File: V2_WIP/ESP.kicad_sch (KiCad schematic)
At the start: 36 parts, among them J202 USB4145-03-0230-C, Q1 IRLML5203, Q2 S8050, Q3 S8050, SW2 PTS647SN70SMTR2N LFS, U1 ESP32-WROOM-32UE, U14 *CH340K, U201 RT9080-33GJ5

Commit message: updated list of changes in README.md
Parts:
- added R108: 1k, Resistor_SMD:R_0603_1608Metric_Pad0.98x0.95mm_HandSolder, symbol Device:R
- TP201: footprint TestPoint:TestPoint_Pad_D1.5mm -> TestPoint:TestPoint_Pad_D1.0mm
- TP202: value VCC -> LDO_VCC; footprint TestPoint:TestPoint_Pad_D1.5mm -> TestPoint:TestPoint_Pad_D1.0mm
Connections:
- net +3V3: now also R108.2
- net GND: now also J202.B8 (SBU2); no longer J202.B5 (CC2)
- net at R205.2: now also J202.B5 (CC2); no longer J202.B8 (SBU2)
- net at U1.29 (IO5): now also R108.1
- no-connect marks 6 -> 5
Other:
- note added: "ENC CLK"
- note added: "ENC DT"
- note added: "ENC SW"
- note added: "GNSS TX"
- note added: "GNSSRX"
- note added: "LED"
- note added: "LIGHT_SENS"
- note added: "PULSE"
- note added: "RGB_DATA"
- note added: "RTS"
- note added: "SEL_FL"
- note added: "SEL_IMU"
- note added: "SW2"
- note added: "TP12"
- moved on the sheet: D7, Q3

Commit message: reworked the schematic, changed differential pairs and RF traces, small PCB adjustments
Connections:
- net D+ renamed D_P
- net D- renamed D_N
- net RXD0 renamed RxD0
- net TXD0 renamed TxD0
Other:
- moved on the sheet: C2, C203, C204

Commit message: added second LDO
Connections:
- net IO34: now reaches U1.6 (IO34)
- net IO33: now reaches U1.9 (IO33)
- net +3V3 renamed +3V3_ESP
- no-connect marks 5 -> 3
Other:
- note added: "IMU_INT"
- note added: "LDO_EN"
- moved on the sheet: C11, C201, C202, C3, D3, D4, Q1, R11, R12, TP202, U201

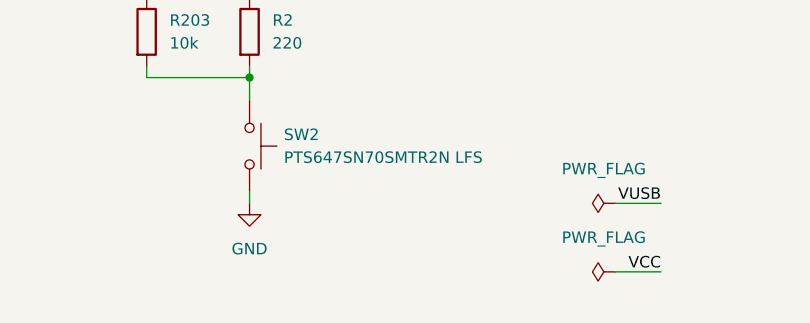
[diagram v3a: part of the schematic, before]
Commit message: switched Tx and Rx on GNSS module, added option to switch them, minor pcb changes
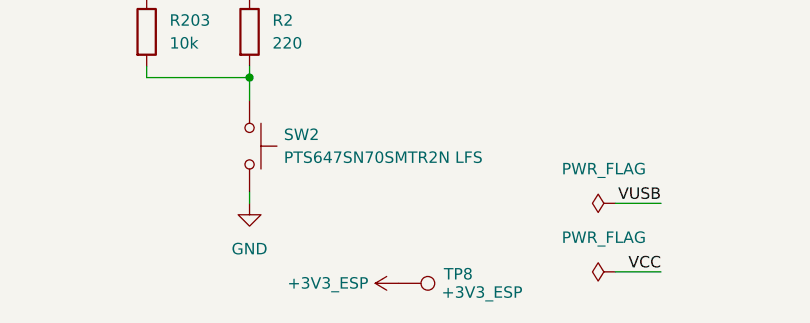
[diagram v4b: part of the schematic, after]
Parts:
- added TP8: +3V3_ESP, TestPoint:TestPoint_Pad_D1.0mm, symbol Connector:TestPoint
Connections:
- net +3V3_ESP: now also TP8.1
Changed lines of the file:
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@@
 	)
 	(symbol
+		(lib_id "Connector:TestPoint")
+		(at 144.78 191.77 270)
+		(unit 1)
+		(body_style 1)
+		(exclude_from_sim no)
+		(in_bom yes)
+		(on_board yes)
+		(in_pos_files yes)
+		(dnp no)
+		(property "Reference" "TP8"
+			(at 149.86 190.754 90)
+			(show_name no)
+			(do_not_autoplace no)
+			(effects
+				(font
+					(size 1.27 1.27)
+				)
+				(justify left)
+			)
+		)
+		(property "Value" "+3V3_ESP"
+			(at 149.606 192.786 90)
+			(show_name no)
+			(do_not_autoplace no)
+			(effects
+				(font
+					(size 1.27 1.27)
+				)
+				(justify left)
+			)
+		)
+		(property "Footprint" "TestPoint:TestPoint_Pad_D1.0mm"
+			(at 144.78 196.85 0)
+			(hide yes)
+			(show_name no)
+			(do_not_autoplace no)
+			(effects
+				(font
+					(size 1.27 1.27)
+				)
+			)
+		)
+		(property "Datasheet" ""
+			(at 144.78 196.85 0)
+			(hide yes)
+			(show_name no)
+			(do_not_autoplace no)
+			(effects
+				(font
+					(size 1.27 1.27)
+				)
+			)
+		)
+		(property "Description" "test point"
+			(at 144.78 191.77 0)
+			(hide yes)
+			(show_name no)
+			(do_not_autoplace no)
+			(effects
+				(font
+					(size 1.27 1.27)
+				)
+			)
+		)
+		(property "Purchase-URL" ""
+			(at 144.78 191.77 0)
+			(hide yes)
+			(show_name no)
+			(do_not_autoplace no)
+			(effects
+				(font
+					(size 1.27 1.27)
+				)
+			)
+		)
+		(pin "1"
+		)
+		(instances
+			(project "gps"
+				(path "/00526ddc-5304-4072-af1e-192a9e7e83da/9ca8f2f0-17b3-4db3-a6cc-93c49e56ea8b"
+					(reference "TP8")
+					(unit 1)
+				)
+			)
+		)
+	)
+	(symbol
 		(lib_id "power:GND")
 		(at 57.15 184.15 0)
@@
 					(unit 1)
 				)
+			)
+		)
+	)
+	(symbol
+		(lib_id "power:+3V3")
+		(at 144.78 191.77 90)
+		(unit 1)
+		(body_style 1)
+		(exclude_from_sim no)
+		(in_bom yes)
+		(on_board yes)
+		(in_pos_files yes)
+		(dnp no)
+		(property "Reference" "#PWR0167"
+			(at 148.59 191.77 0)
+			(hide yes)
+			(show_name no)
+			(do_not_autoplace no)
+			(effects
+				(font
+					(size 1.27 1.27)
+				)
+			)
+		)
+		(property "Value" "+3V3_ESP"
+			(at 141.478 191.77 90)
+			(show_name no)
+			(do_not_autoplace no)
+			(effects
+				(font
+					(size 1.27 1.27)
+				)
+				(justify left)
+			)
+		)
+		(property "Footprint" ""
+			(at 144.78 191.77 0)
+			(hide yes)
+			(show_name no)
+			(do_not_autoplace no)
+			(effects
+				(font
+					(size 1.27 1.27)
+				)
+			)
+		)
+		(property "Datasheet" ""
+			(at 144.78 191.77 0)
+			(hide yes)
+			(show_name no)
+			(do_not_autoplace no)
+			(effects
+				(font
+					(size 1.27 1.27)
+				)
+			)
+		)
+		(property "Description" "Power symbol creates a global label with name \"+3V3\""
+			(at 144.78 191.77 0)
+			(hide yes)
+			(show_name no)
+			(do_not_autoplace no)
+			(effects
+				(font
+					(size 1.27 1.27)
+				)
+			)
+		)
+		(pin "1"
+		)
+		(instances
+			(project "gps"
+				(path "/00526ddc-5304-4072-af1e-192a9e7e83da/9ca8f2f0-17b3-4db3-a6cc-93c49e56ea8b"
+					(reference "#PWR0167")
+					(unit 1)
+				)

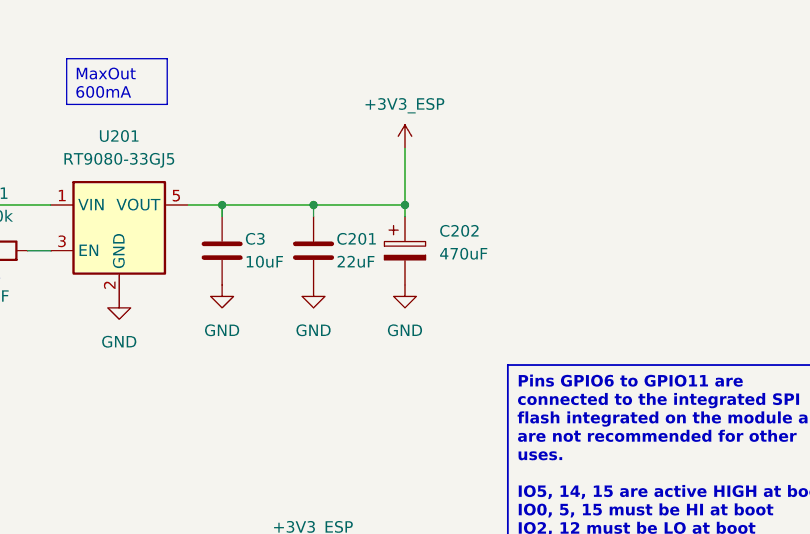
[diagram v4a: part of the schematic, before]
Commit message: adjusted elec capacitors
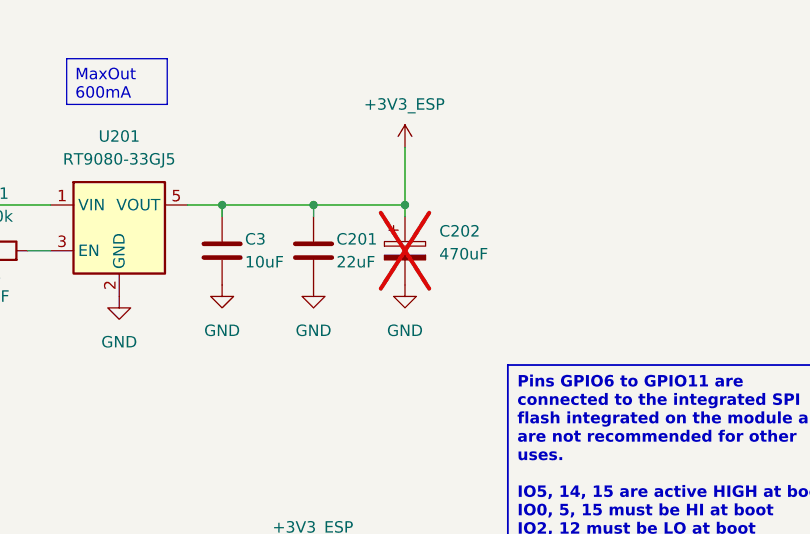
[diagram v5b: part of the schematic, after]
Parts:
- C202: now not fitted
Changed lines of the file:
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@@
 		(on_board yes)
 		(in_pos_files yes)
-		(dnp no)
+		(dnp yes)
 		(fields_autoplaced yes)
 		(property "Reference" "C202"
